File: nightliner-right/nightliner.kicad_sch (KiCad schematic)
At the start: 86 parts, among them J1 TYPE-C-31-M-12, J2 Battery, J3 Serial, J4 Battery, P1 ISP_Prog, SW1 pinky_top, SW10 inner_home, SW11 pinky_bottom, SW12 ring_bottom, SW13 middle_bottom, SW14 index_bottom, SW15 inner_bottom, SW16 outer_top, SW17 outer_home, SW18 near_thumb, SW19 home_thumb, SW2 ring_top, SW20 far_thumb, SW21 ON_OFF, SW22 RESET, SW3 middle_top, SW4 index_top, SW5 inner_top, SW6 pinky_home, SW7 ring_home, SW8 middle_home, SW9 index_home, U1 holyiot-18010, U2 TVS2200DRV, U3 USBLC6-2SC6, U4 BQ24075RGT, U5 XC6220B331MR

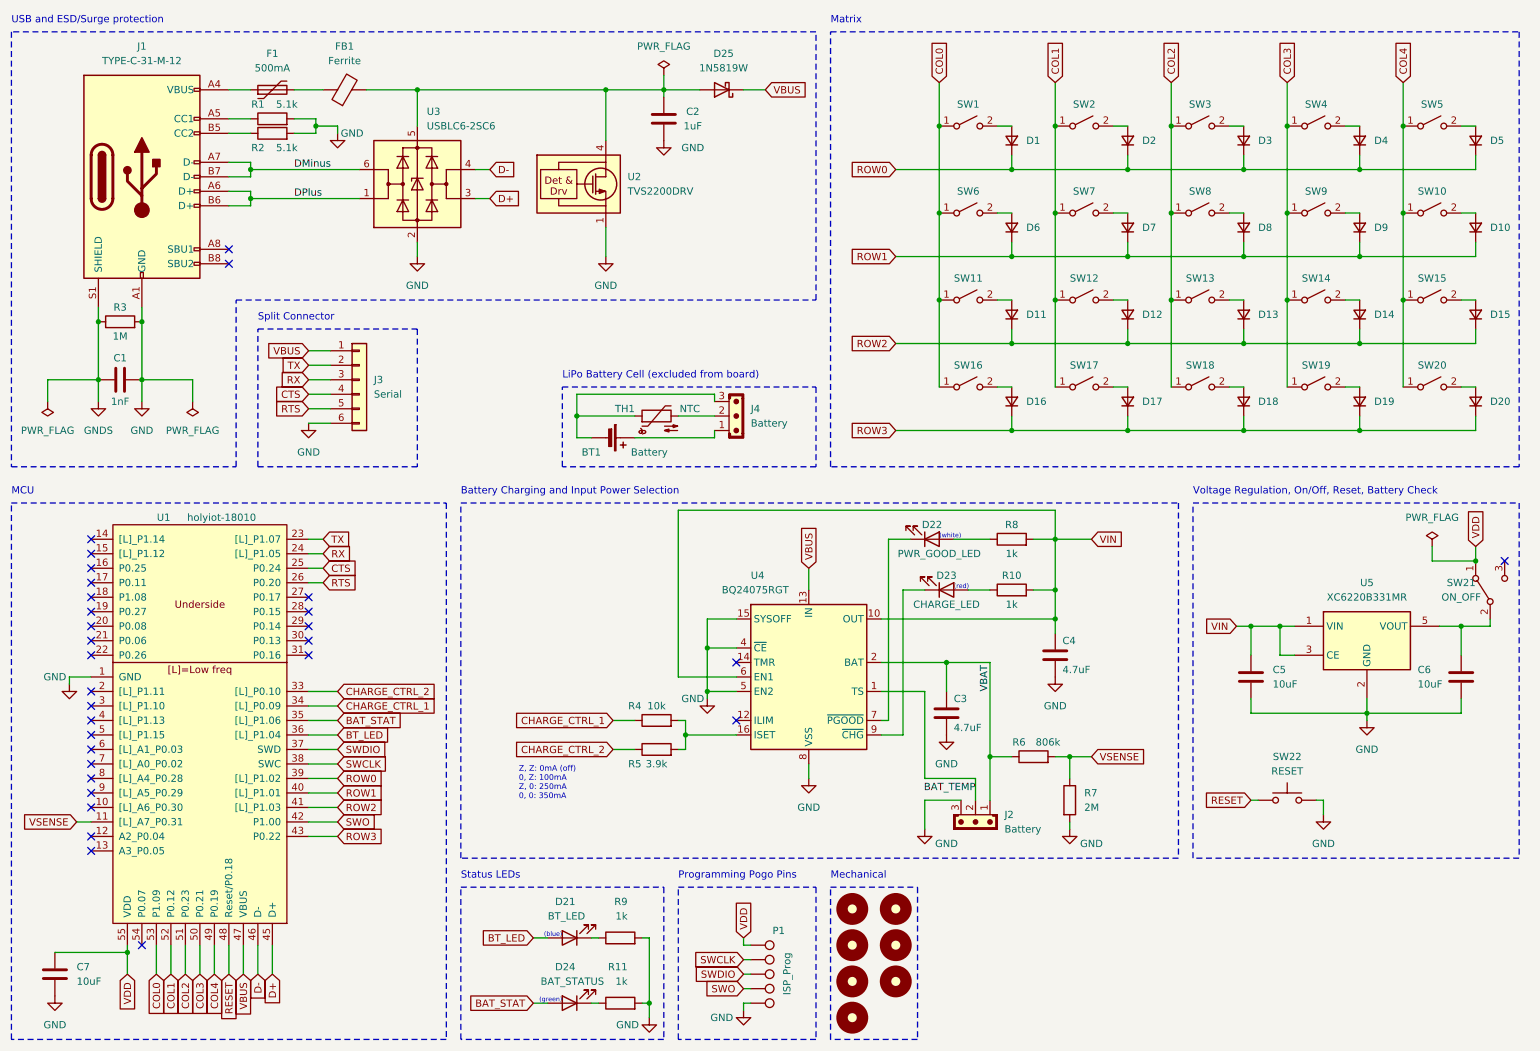
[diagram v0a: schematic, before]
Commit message: fix: make sides symmetric
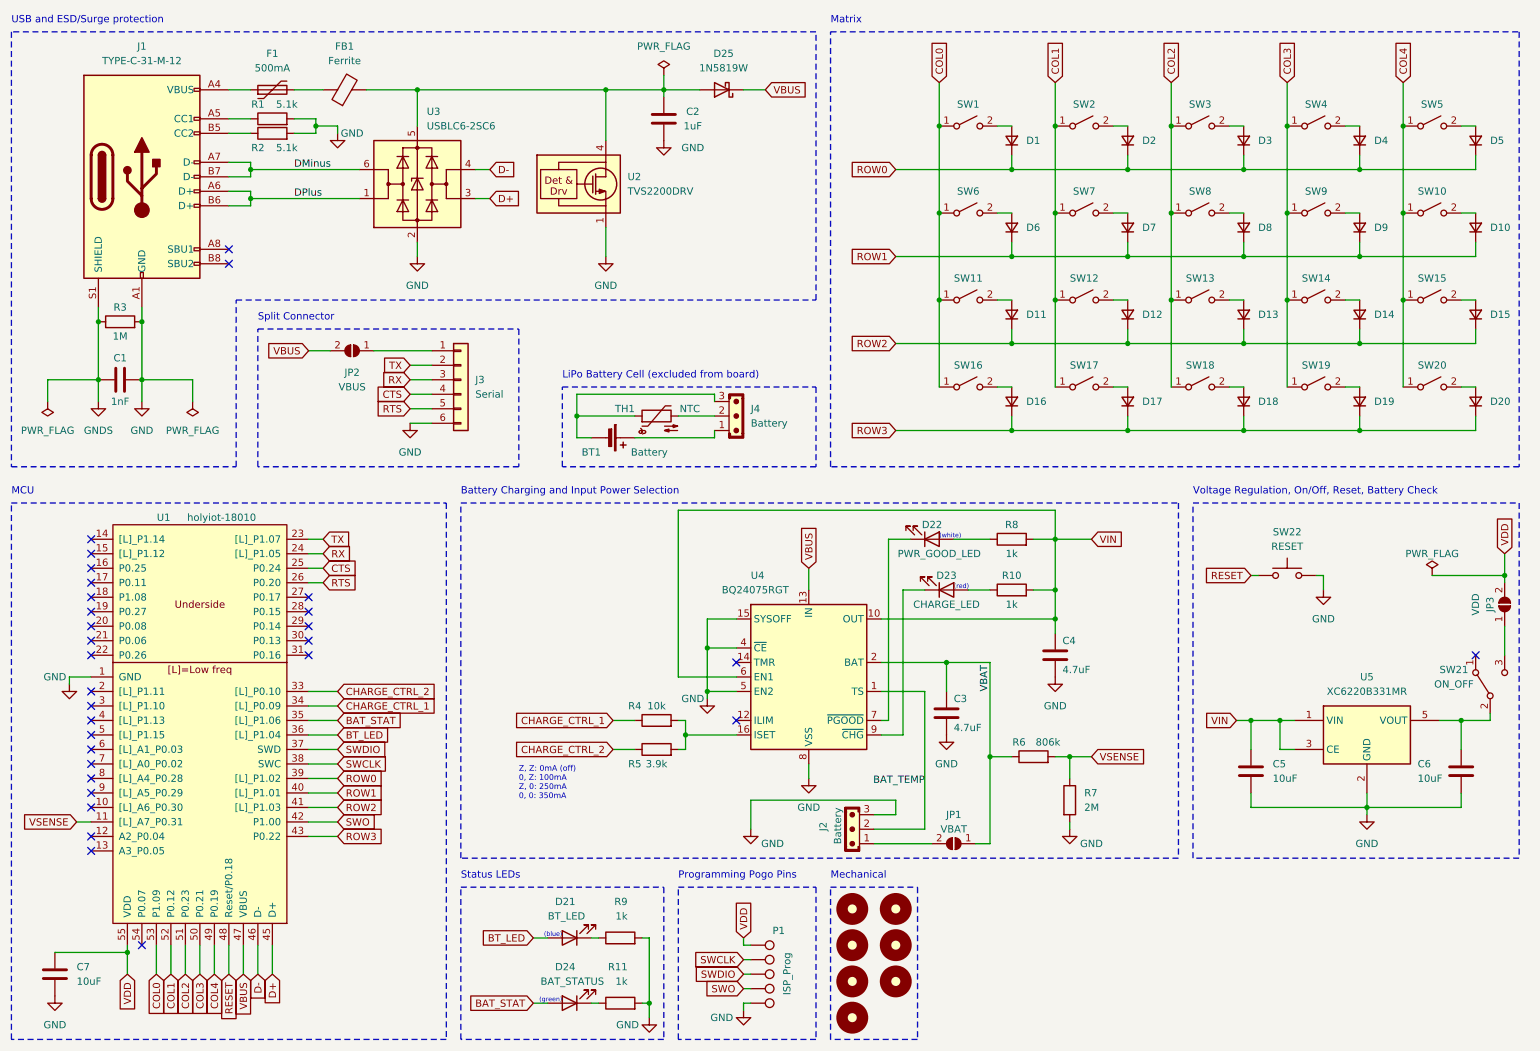
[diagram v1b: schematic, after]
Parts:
- added JP1: VBAT, Jumper:SolderJumper-2_P1.3mm_Open_RoundedPad1.0x1.5mm, symbol Jumper:SolderJumper_2_Open
- added JP2: VBUS, Jumper:SolderJumper-2_P1.3mm_Open_RoundedPad1.0x1.5mm, symbol Jumper:SolderJumper_2_Open
- added JP3: VDD, Jumper:SolderJumper-2_P1.3mm_Open_RoundedPad1.0x1.5mm, symbol Jumper:SolderJumper_2_Open
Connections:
- net VBAT: now also JP1.1 (A); no longer J2.1
- net VBUS: now also JP2.2 (B); no longer J3.1 (Pin_1)
- net VDD: now also JP3.2 (B); no longer SW21.1 (A)
- net at SW21.3 (C): now also JP3.1 (A)
- new net: J3.1 (Pin_1), JP2.1 (A)
- new net: J2.1, JP1.2 (B)
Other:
- moved on the sheet: C5, C6, J2, J3, SW21, SW22, U5

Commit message: fix: change edge outline, flip switches
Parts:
- added JP4: VBUS, Jumper:SolderJumper-2_P1.3mm_Open_RoundedPad1.0x1.5mm, symbol Jumper:SolderJumper_2_Open
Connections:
- net VBUS: now also JP4.1 (A); no longer U1.47 (VBUS)
- net at SW21.1 (A): now also JP3.1 (A)
- net at SW21.3 (C): no longer JP3.1 (A)
- new net: JP4.2 (B), U1.47 (VBUS)
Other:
- moved on the sheet: JP3
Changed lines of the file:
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@@
   (junction (at 199.39 49.53) (diameter 0) (color 0 0 0 0)
   )
-  (junction (at 278.13 113.03) (diameter 0) (color 0 0 0 0)
+  (junction (at 273.05 113.03) (diameter 0) (color 0 0 0 0)
   )
   (junction (at 232.41 87.63) (diameter 0) (color 0 0 0 0)
@@
   (no_connect (at 68.58 119.38))
   (no_connect (at 68.58 116.84))
-  (no_connect (at 273.05 127))
+  (no_connect (at 278.13 127))
   (no_connect (at 30.48 116.84))
   (no_connect (at 30.48 133.35))
@@
     (stroke (width 0) (type default))
   )
-  (wire (pts (xy 278.13 109.22) (xy 278.13 113.03))
+  (wire (pts (xy 273.05 109.22) (xy 273.05 113.03))
     (stroke (width 0) (type default))
   )
@@
     (stroke (width 0) (type default))
   )
+  (wire (pts (xy 76.2 190.5) (xy 80.01 190.5))
+    (stroke (width 0) (type default))
+  )
   (wire (pts (xy 69.85 34.29) (xy 69.85 35.56))
     (stroke (width 0) (type default))
@@
     (stroke (width 0) (type default))
   )
-  (wire (pts (xy 278.13 114.3) (xy 278.13 113.03))
+  (wire (pts (xy 273.05 114.3) (xy 273.05 113.03))
     (stroke (width 0) (type default))
   )
@@
     (stroke (width 0) (type default))
   )
+  (wire (pts (xy 68.58 190.5) (xy 57.15 190.5))
+    (stroke (width 0) (type default))
+  )
   (wire (pts (xy 252.73 39.37) (xy 252.73 41.91))
     (stroke (width 0) (type default))
@@
     (stroke (width 0) (type default))
   )
-  (wire (pts (xy 278.13 121.92) (xy 278.13 127))
-    (stroke (width 0) (type default))
-  )
   (wire (pts (xy 68.58 143.51) (xy 73.66 143.51))
     (stroke (width 0) (type default))
@@
     (stroke (width 0) (type default))
   )
+  (wire (pts (xy 273.05 121.92) (xy 273.05 127))
+    (stroke (width 0) (type default))
+  )
   (wire (pts (xy 171.45 41.91) (xy 191.77 41.91))
     (stroke (width 0) (type default))
   )
-  (wire (pts (xy 265.43 113.03) (xy 278.13 113.03))
+  (wire (pts (xy 260.35 113.03) (xy 273.05 113.03))
     (stroke (width 0) (type default))
   )
@@
     (stroke (width 0) (type default))
   )
+  (wire (pts (xy 57.15 177.8) (xy 57.15 190.5))
+    (stroke (width 0) (type default))
+  )
   (wire (pts (xy 62.23 177.8) (xy 62.23 182.88))
     (stroke (width 0) (type default))
@@
     (stroke (width 0) (type default))
   )
-  (wire (pts (xy 57.15 177.8) (xy 57.15 182.88))
-    (stroke (width 0) (type default))
-  )
   (wire (pts (xy 176.53 133.35) (xy 176.53 157.48))
     (stroke (width 0) (type default))
@@
     )
   )
-  (global_label "VBUS" (shape input) (at 57.15 182.88 270) (fields_autoplaced)
-    (effects (font (size 1.27 1.27)) (justify right))
-    (property "Intersheetrefs" "${INTERSHEET_REFS}" (at 57.15 190.7638 90)
-      (effects (font (size 1.27 1.27)) (justify right) hide)
+  (global_label "VBUS" (shape input) (at 80.01 190.5 0) (fields_autoplaced)
+    (effects (font (size 1.27 1.27)) (justify left))
+    (property "Intersheetrefs" "${INTERSHEET_REFS}" (at 87.8938 190.5 0)
+      (effects (font (size 1.27 1.27)) (justify left) hide)
     )
   )
-  (global_label "VDD" (shape input) (at 278.13 109.22 90) (fields_autoplaced)
+  (global_label "VDD" (shape input) (at 273.05 109.22 90) (fields_autoplaced)
     (effects (font (size 1.27 1.27)) (justify left))
-    (property "Intersheetrefs" "${INTERSHEET_REFS}" (at 278.13 102.6062 90)
+    (property "Intersheetrefs" "${INTERSHEET_REFS}" (at 273.05 102.6062 90)
       (effects (font (size 1.27 1.27)) (justify left) hide)
     )
@@
     )
   )
-  (symbol (lib_id "power:PWR_FLAG") (at 265.43 113.03 0) (unit 1)
+  (symbol (lib_id "power:PWR_FLAG") (at 260.35 113.03 0) (unit 1)
     (in_bom yes) (on_board yes) (dnp no)
-    (property "Reference" "#FLG03" (at 265.43 111.125 0)
+    (property "Reference" "#FLG03" (at 260.35 111.125 0)
       (effects (font (size 1.27 1.27)) hide)
     )
-    (property "Value" "PWR_FLAG" (at 265.43 109.22 0)
+    (property "Value" "PWR_FLAG" (at 260.35 109.22 0)
       (effects (font (size 1.27 1.27)))
     )
-    (property "Footprint" "" (at 265.43 113.03 0)
+    (property "Footprint" "" (at 260.35 113.03 0)
       (effects (font (size 1.27 1.27)) hide)
     )
-    (property "Datasheet" "~" (at 265.43 113.03 0)
+    (property "Datasheet" "~" (at 260.35 113.03 0)
       (effects (font (size 1.27 1.27)) hide)
     )
@@
     )
   )
-  (symbol (lib_id "Jumper:SolderJumper_2_Open") (at 278.13 118.11 90) (unit 1)
+  (symbol (lib_id "Jumper:SolderJumper_2_Open") (at 273.05 118.11 90) (unit 1)
     (in_bom yes) (on_board yes) (dnp no)
-    (property "Reference" "JP3" (at 275.59 118.11 0)
+    (property "Reference" "JP3" (at 270.51 118.11 0)
       (effects (font (size 1.27 1.27)))
     )
-    (property "Value" "VDD" (at 273.05 118.11 0)
+    (property "Value" "VDD" (at 267.97 118.11 0)
       (effects (font (size 1.27 1.27)))
     )
-    (property "Footprint" "Jumper:SolderJumper-2_P1.3mm_Open_RoundedPad1.0x1.5mm" (at 278.13 118.11 0)
+    (property "Footprint" "Jumper:SolderJumper-2_P1.3mm_Open_RoundedPad1.0x1.5mm" (at 273.05 118.11 0)
       (effects (font (size 1.27 1.27)) hide)
     )
-    (property "Datasheet" "~" (at 278.13 118.11 0)
+    (property "Datasheet" "~" (at 273.05 118.11 0)
       (effects (font (size 1.27 1.27)) hide)
     )
-    (property "PartNumber" "" (at 278.13 118.11 0)
+    (property "PartNumber" "" (at 273.05 118.11 0)
       (effects (font (size 1.27 1.27)) hide)
     )
-    (property "LCSCNumber" "" (at 278.13 118.11 0)
+    (property "LCSCNumber" "" (at 273.05 118.11 0)
       (effects (font (size 1.27 1.27)) hide)
     )
@@
         )
       )
+    )
+  )
+  (symbol (lib_id "Jumper:SolderJumper_2_Open") (at 72.39 190.5 180) (unit 1)
+    (in_bom yes) (on_board yes) (dnp no)
+    (property "Reference" "JP4" (at 72.39 187.96 0)
+      (effects (font (size 1.27 1.27)))
+    )
+    (property "Value" "VBUS" (at 72.39 185.42 0)
+      (effects (font (size 1.27 1.27)))
+    )
+    (property "Footprint" "Jumper:SolderJumper-2_P1.3mm_Open_RoundedPad1.0x1.5mm" (at 72.39 190.5 0)
+      (effects (font (size 1.27 1.27)) hide)
+    )
+    (property "Datasheet" "~" (at 72.39 190.5 0)
+      (effects (font (size 1.27 1.27)) hide)
+    )
+    (property "PartNumber" "" (at 72.39 190.5 0)
+      (effects (font (size 1.27 1.27)) hide)
+    )
+    (property "LCSCNumber" "" (at 72.39 190.5 0)
+      (effects (font (size 1.27 1.27)) hide)
+    )
+    (pin "1")
+    (pin "2")
+    (instances
+      (project "nightliner"
+        (path "/e4693d91-d111-4059-a601-28406aaad775"
+          (reference "JP4") (unit 1)
+        )
+      )

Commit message: fix: final version, create production gerbers
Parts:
- C1: LCSCNumber (none) -> C94121; PartNumber (none) -> CC0805KRX7R9BB102
- C2: LCSCNumber (none) -> C91186; PartNumber (none) -> CC0805KKX7R8BB105
- C3, C4: LCSCNumber (none) -> C354262; PartNumber (none) -> CC0805KKX7R8BB475
- C5, C6, C7: LCSCNumber (none) -> C89831; PartNumber (none) -> CC0805KKX5R8BB106
- D1, D10, D11, D12, D13, D14, D15, D16, D17, D18, D19, D2, D20, D3, D4, D5, D6, D7, D8, D9: value D_Small -> 1N4148WS; LCSCNumber (none) -> C5345963; PartNumber (none) -> 1N4148WS
- D25: LCSCNumber (none) -> C727115; PartNumber (none) -> 1N5819W
- H1: footprint miro_keyboard:StandOff_6mm_M3 -> nightliner:StandOff_6mm_M3
- H2, H3, H4, H5, H6, H7: value MountingHole_M3 -> Standoff_6mm_M3; footprint miro_keyboard:StandOff_6mm_M3 -> nightliner:StandOff_6mm_M3
- J1: symbol Connector:USB_C_Receptacle_USB2.0 -> nightliner:USB_C_Receptacle_USB2.0
- J2: LCSCNumber (none) -> C163036; PartNumber (none) -> S3B-XH-A-1(LF)(SN)
- J3: footprint miro_keyboard:MagConn_6pin_right -> nightliner:MagConn_6pin_right
- P1: footprint miro_keyboard:ISP_Programming_Pads -> nightliner:ISP_Programming_Pads
- R1, R2: LCSCNumber (none) -> C144553; PartNumber (none) -> AC0805FR-075K1L
- R10, R11, R8, R9: LCSCNumber (none) -> C95781; PartNumber (none) -> RC0805FR-071KL
- R3: LCSCNumber (none) -> C107700; PartNumber (none) -> RC0805FR-071ML
- R4: LCSCNumber (none) -> C140868; PartNumber (none) -> AC0805FR-0710KL
- R6: LCSCNumber (none) -> C273852; PartNumber (none) -> RC0805FR-07806KL
- R7: LCSCNumber (none) -> C114532; PartNumber (none) -> RC0805FR-072ML
- SW1, SW10, SW11, SW12, SW13, SW14, SW15, SW16, SW17, SW18, SW19, SW2, SW20, SW3, SW4, SW5, SW6, SW7, SW8, SW9: footprint miro_keyboard:Kailh_Choc_CPG135001D02_Hotswap -> nightliner:Kailh_Choc_CPG135001D02_Hotswap
- SW21: footprint miro_keyboard:SW_ROCPU_SK-12D07-5_SPDT_Angled -> nightliner:SW_ROCPU_SK-12D07-5_SPDT_Angled; LCSCNumber (none) -> C2857676; PartNumber (none) -> SK-12D07-5
- SW22: footprint miro_keyboard:SW_Push_1P1T_NO_CK_KSC4xxJ -> nightliner:SW_Push_1P1T_NO_CK_KSC4xxJ
- U1: footprint miro_keyboard:HOLYIOT-18010-UndersidePins-SMD -> nightliner:HOLYIOT-18010-UndersidePins-SMD
- U2: LCSCNumber (none) -> C523793; PartNumber (none) -> TVS2200DRVR
- U3: LCSCNumber (none) -> C7519; PartNumber (none) -> USBLC6-2SC6
- U4: footprint miro_keyboard:VQFN-16-1EP_3x3mm_P0.5mm_EP1.6x1.6mm_ThermalVias -> nightliner:VQFN-16-1EP_3x3mm_P0.5mm_EP1.6x1.6mm_ThermalVias; LCSCNumber (none) -> C15464; PartNumber (none) -> BQ24075RGTR
- U5: LCSCNumber (none) -> C86534; PartNumber (none) -> XC6220B331MR-G
